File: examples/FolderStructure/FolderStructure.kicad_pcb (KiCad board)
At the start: 2 copper layers, 45.8 x 33.3 mm, 13 parts, among them M1 Motor_DC, M2 Motor_DC, M3 Motor_DC, Q1 MMBT2222A, Q2 MMBT2222A, Q3 MMBT2222A, U1 ATtiny1626-X

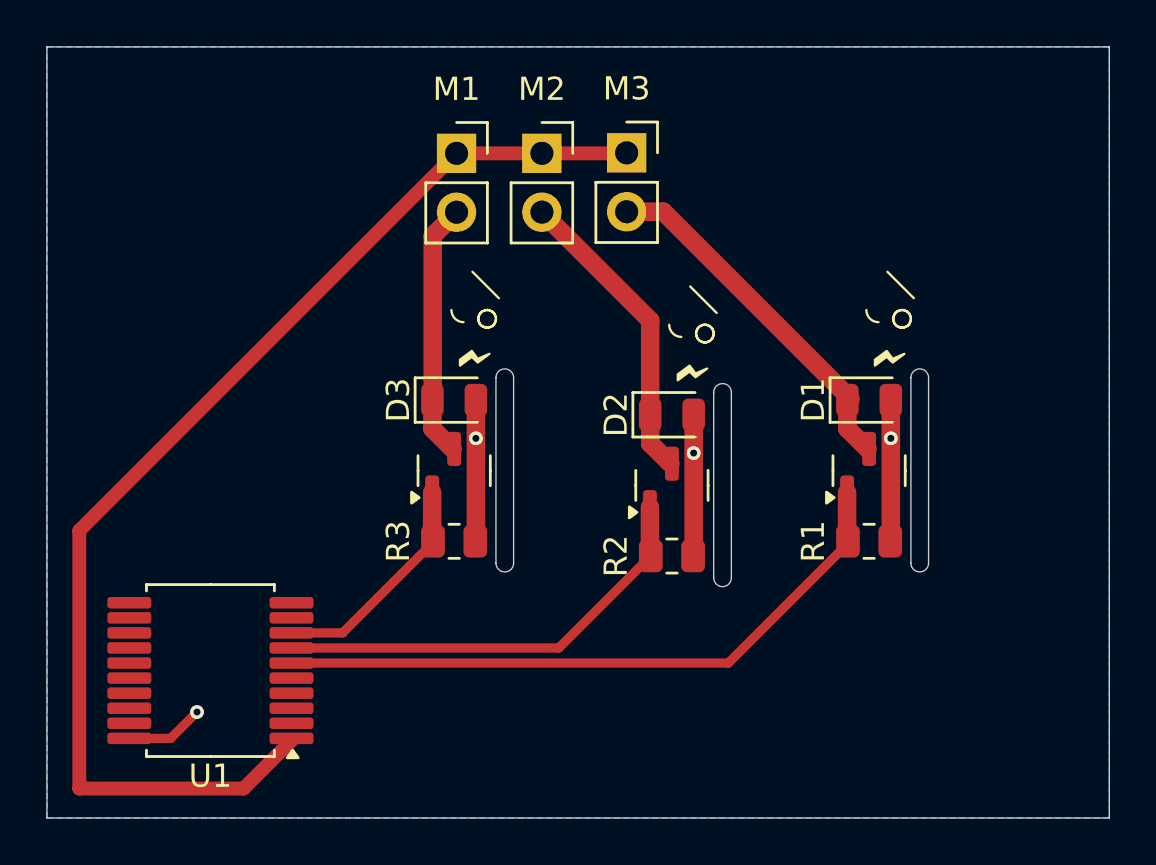
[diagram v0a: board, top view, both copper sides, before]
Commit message: Add Zones to Examples
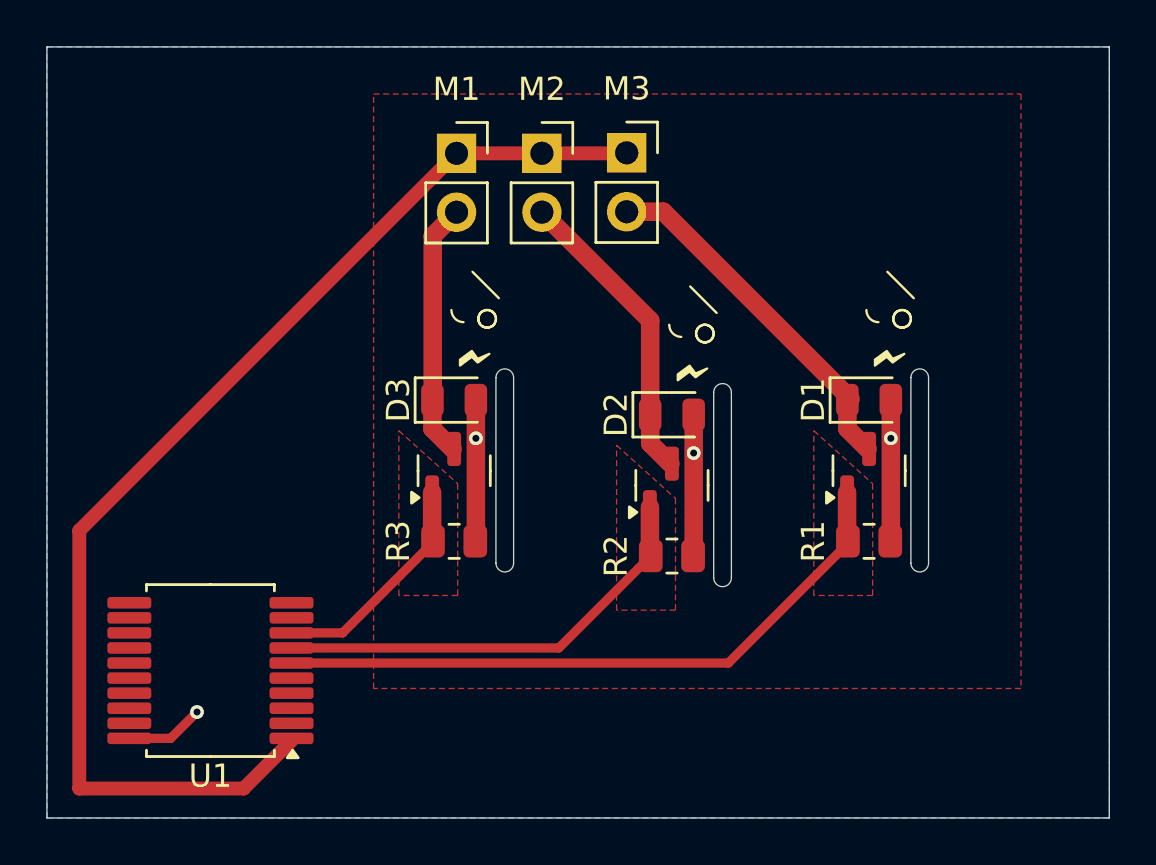
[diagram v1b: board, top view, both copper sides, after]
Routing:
- added copper zone on F.Cu, net /Sinking Digital/Input
- added copper zone on F.Cu, net /Sinking Digital1/Input
- added copper zone on F.Cu, net /Sinking Digital2/Input
- added copper zone on F.Cu, net GND
